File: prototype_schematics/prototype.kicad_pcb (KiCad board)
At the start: 2 copper layers, 3.7 x 6.9 mm, 98 parts, among them J1 AudioJack3, J2 Conn_01x04, J3 Conn_Coaxial, U1 MAX2608EUT+T, U10 TA0411A, U2 SPX3819M5-L, U3 TLV61046ADB, U4 MAX2680AUT+, U5 CD74HC4046A, U6 BGA2802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

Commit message: layout wip
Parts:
- J3: footprint Connector_Coaxial:SMA_Wurth_60312002114503_Vertical -> Connector_Coaxial:SMA_Samtec_SMA-J-P-X-ST-EM1_EdgeMount
- L12: footprint Inductor_SMD:L_0201_0603Metric_Pad0.64x0.40mm_HandSolder -> Inductor_SMD:L_0603_1608Metric_Pad1.05x0.95mm_HandSolder
- TP1, TP2, TP3, TP4, TP5, TP6: footprint CONMHF1_SMD_T:CONN_CONMHF1-SMD_LNX -> Connector_Coaxial:U.FL_Molex_MCRF_73412-0110_Vertical
- U6: footprint Package_TO_SOT_SMD:SOT-363_SC-70-6 -> Package_TO_SOT_SMD:SOT-363_SC-70-6_Handsoldering
- moved L12 86.9 mm to (61.5, 141.4), turned to 90 degrees
- moved U10 82.6 mm to (67.5, 139.0), turned to -90 degrees
- moved U9 82.0 mm to (60.9, 136.6), turned to 90 degrees
- moved TP5 78.6 mm to (71.5, 146.0), turned to 180 degrees
- moved C36 77.1 mm to (59.0, 134.5)
- moved C37 74.9 mm to (62.6, 138.8)
- moved L9 74.1 mm to (74.0, 139.0), turned to 180 degrees
- moved L8 73.3 mm to (77.5, 139.0), turned to 180 degrees
- moved RV2 72.4 mm to (62.0, 121.5), turned to 90 degrees
- moved C23 70.9 mm to (86.5, 141.6), turned to -90 degrees
- moved C38 67.9 mm to (71.5, 141.5), turned to -90 degrees
- moved L3 64.6 mm to (75.6, 120.5), turned to 180 degrees
- moved C16 64.0 mm to (80.0, 136.5), turned to 90 degrees
- moved C19 62.0 mm to (80.0, 141.5), turned to -90 degrees
- moved R15 60.7 mm to (83.5, 139.0), turned to 180 degrees
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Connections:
- C1 pad 2: Net-(U4-LO) -> Net-(TP1-In)
- C9 pad 2: Net-(TP1-In) -> Net-(U4-LO)
- R9 pad 1: Net-(Y1-OUT/IN) -> GND
- R9 pad 2: GND -> Net-(U5-SigIn)

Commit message: wip layout
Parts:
- added C40: 1nF, Capacitor_SMD:C_0603_1608Metric_Pad1.08x0.95mm_HandSolder, F.Cu at (101.5, 123.0)
- J2: footprint Connector_JST:JST_PH_S4B-PH-K_1x04_P2.00mm_Horizontal -> Connector_PinHeader_2.54mm:PinHeader_1x04_P2.54mm_Vertical
- moved TP6 90.8 mm to (63.0, 146.0), turned to 180 degrees
- moved C39 89.0 mm to (63.0, 141.5), turned to 90 degrees
- moved J1 77.9 mm to (63.2, 97.3), turned to 90 degrees
- moved U7 66.4 mm to (80.5, 97.5), turned to 180 degrees
- moved C29 59.1 mm to (80.5, 102.0)
- moved C27 58.7 mm to (97.5, 139.0), turned to -90 degrees
- moved TP3 58.0 mm to (86.5, 146.0), turned to 180 degrees
- moved TP4 52.4 mm to (97.5, 143.5), turned to 180 degrees
- moved L11 52.3 mm to (103.0, 134.5)
- moved JP3 51.1 mm to (88.5, 113.5), turned to 180 degrees
- moved JP2 51.0 mm to (88.5, 111.0), turned to 180 degrees
- moved JP1 51.0 mm to (88.5, 108.5), turned to 180 degrees
- moved C14 49.1 mm to (89.5, 120.0), turned to -90 degrees
- moved C21 45.3 mm to (100.0, 106.0)
- moved R8 43.4 mm to (89.5, 125.0), turned to -90 degrees
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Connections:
- C10 pad 2: Net-(Y1-OUT/IN) -> Net-(C10-Pad2)
- J2 pad 3: /AFOUT_P -> /AFOUT_N
- J2 pad 4: /AFOUT_N -> /AFOUT_P
- L5 pad 1: Net-(Y1-OUT/IN) -> Net-(C10-Pad2)
- R9 pad 1: GND -> Net-(Y1-OUT/IN)
- R9 pad 2: Net-(U5-SigIn) -> GND
- RV3 pad 1: Net-(R17-Pad2) -> Net-(R18-Pad1)
- RV3 pad 3: Net-(R18-Pad1) -> Net-(R17-Pad2)
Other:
- board size 3.7 x 6.9 mm -> 6.9 x 3.7 mm

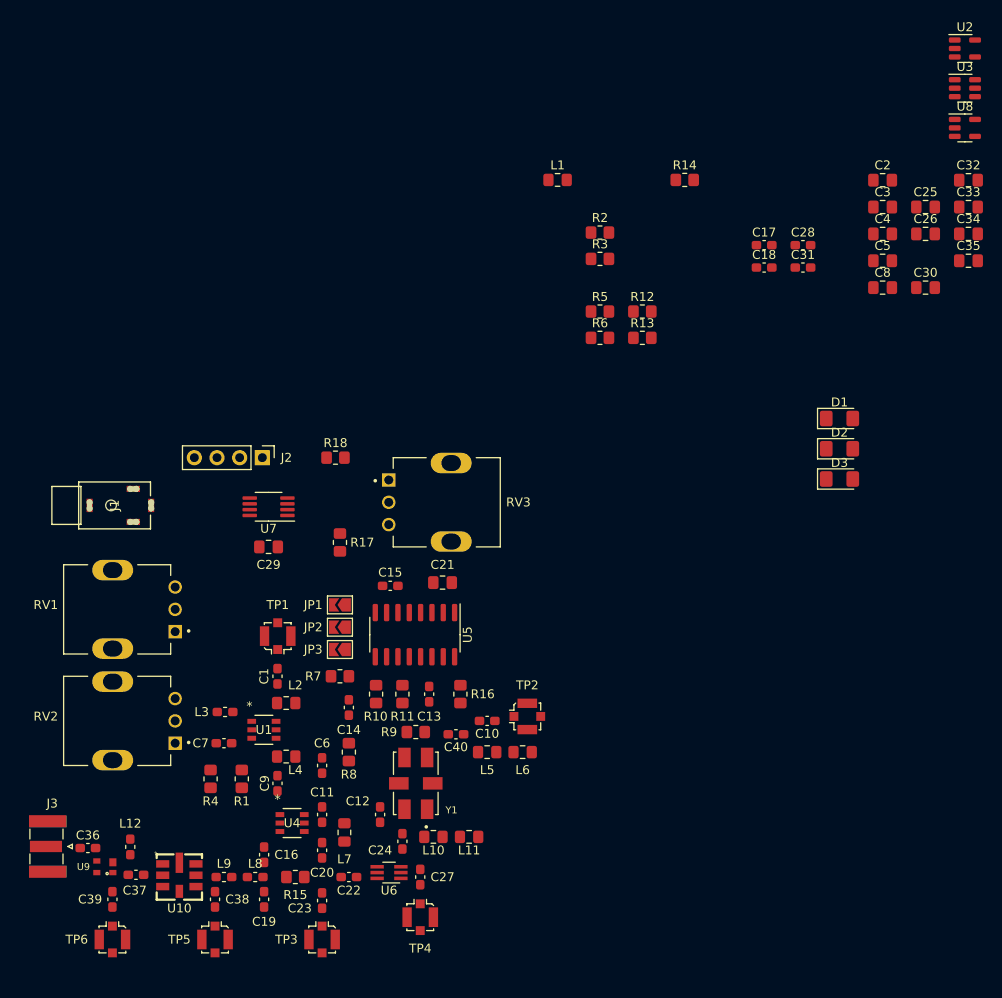
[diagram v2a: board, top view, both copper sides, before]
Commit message: preliminary layout finished
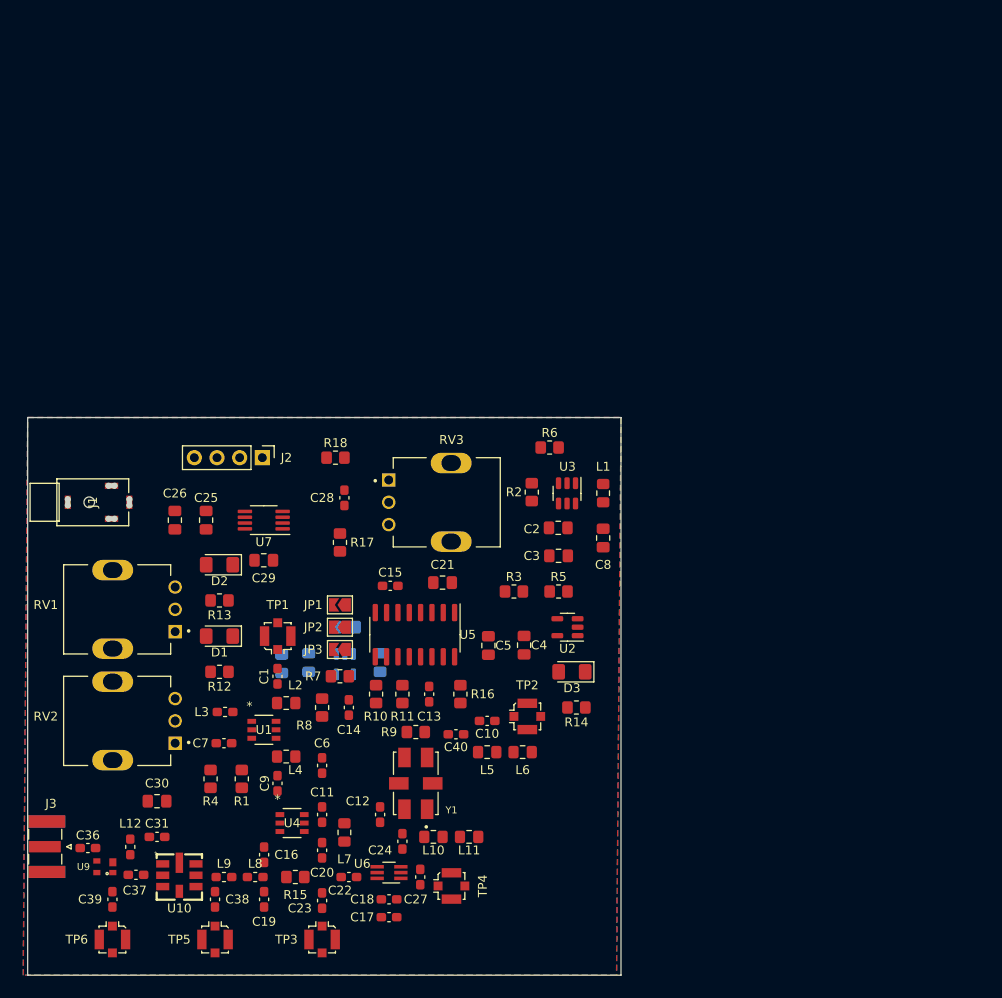
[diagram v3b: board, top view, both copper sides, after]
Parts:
- C32, C33, C34, C35, U8: moved to B.Cu
- moved C30 103.6 mm to (68.0, 130.5), turned to 180 degrees
- moved C31 96.5 mm to (68.0, 134.5), turned to 180 degrees
- moved U8 91.9 mm to (89.0, 115.1), turned to -90 degrees
- moved C26 90.0 mm to (70.0, 99.0), turned to -90 degrees
- moved C35 89.2 mm to (82.0, 115.1), turned to 90 degrees
- moved C34 88.2 mm to (85.0, 115.0), turned to 90 degrees
- moved C25 87.9 mm to (73.5, 99.0), turned to -90 degrees
- moved C17 86.3 mm to (94.0, 143.5), turned to 180 degrees
- moved C32 85.9 mm to (89.2, 111.0), turned to 180 degrees
- moved C33 83.4 mm to (93.0, 115.0), turned to 90 degrees
- moved C18 82.4 mm to (94.0, 141.5), turned to 180 degrees
- moved U2 78.7 mm to (114.0, 111.0), turned to 180 degrees
- moved D1 73.6 mm to (75.0, 112.0), turned to 180 degrees
- moved D2 70.7 mm to (75.0, 104.0), turned to 180 degrees
- moved U3 63.6 mm to (114.0, 96.0), turned to -90 degrees
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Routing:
- added copper zone on B.Cu, net GND
- added copper zone on F.Cu, net GND
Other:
- board size 6.9 x 3.7 mm -> 66.5 x 62.5 mm

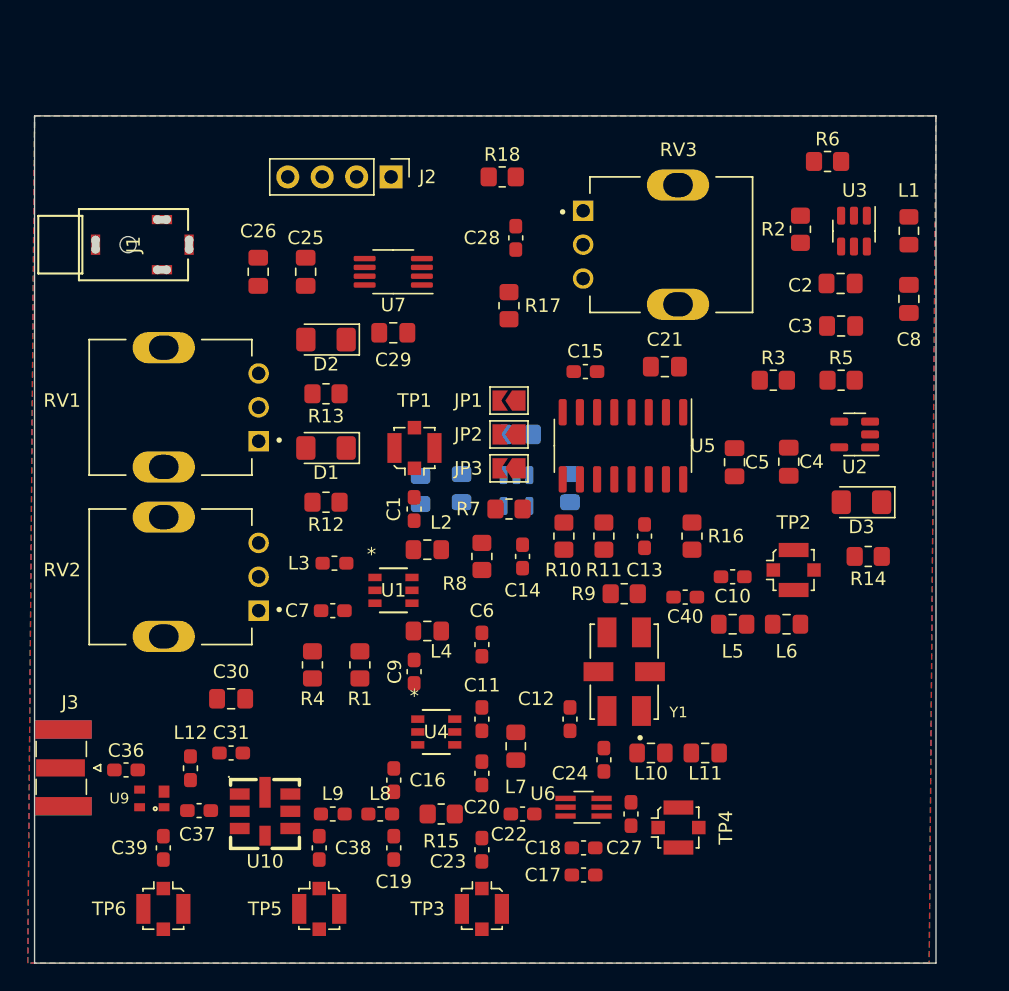
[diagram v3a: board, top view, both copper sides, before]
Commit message: layout adjustment and edge cut
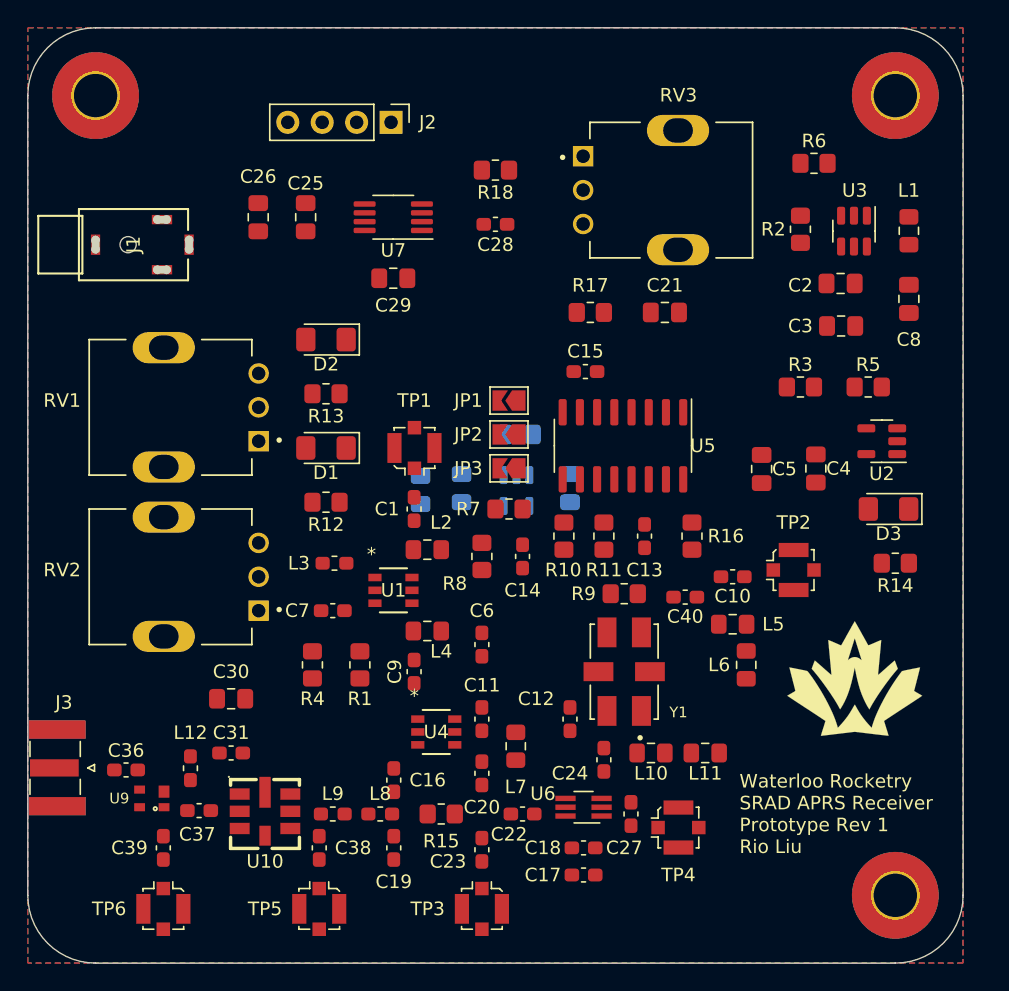
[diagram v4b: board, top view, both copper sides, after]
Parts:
- added G***: LOGO, Team_Logo:Logo_SilkScreen_10mm, F.Cu at (114.0, 129.0)
- added H1: MountingHole_Pad, MountingHole:MountingHole_3.2mm_M3_Pad_TopBottom, F.Cu at (58.0, 86.0)
- added H2: MountingHole_Pad, MountingHole:MountingHole_3.2mm_M3_Pad_TopBottom, F.Cu at (117.0, 86.0)
- added H3: MountingHole_Pad, MountingHole:MountingHole_3.2mm_M3_Pad_TopBottom, F.Cu at (117.0, 145.0)
- moved R17 6.02 mm to (94.5, 102.0), turned to 180 degrees
- moved L6 4.22 mm to (106.0, 128.0), turned to -90 degrees
- moved C25 4.03 mm to (73.5, 95.0)
- moved C26 4.03 mm to (70.0, 95.0)
- moved C29 4.03 mm to (80.0, 99.5)
- moved J2 4.03 mm to (79.8, 88.0)
- moved RV3 4.03 mm to (101.0, 93.0)
- moved U7 4.03 mm to (80.0, 95.0)
- moved C21 4.00 mm to (100.0, 102.0)
- moved C4 2.06 mm to (111.1, 113.5)
- moved C5 2.06 mm to (107.1, 113.5)
- moved D3 2.06 mm to (116.5, 116.5)
- moved R14 2.06 mm to (117.0, 120.5)
- moved R3 2.06 mm to (110.0, 107.5)
- moved R5 2.06 mm to (115.0, 107.5)
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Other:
- board size 66.5 x 62.5 mm -> 69 x 69 mm
- board text added: "Waterloo Rocketry SRAD APRS Receiver Prototype Rev 1 Rio Liu"

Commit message: wip routing
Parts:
- moved R16 23.9 mm to (83.0, 104.0), turned to 180 degrees
- moved C21 12.5 mm to (87.5, 101.5), turned to 180 degrees
- moved U7 6.48 mm to (73.8, 93.0)
- moved C29 6.47 mm to (80.5, 93.0), turned to 180 degrees
- moved C25 4.20 mm to (75.8, 98.5)
- moved C26 4.20 mm to (72.2, 98.5)
- moved JP2 2.50 mm to (88.5, 113.5)
- moved JP3 2.50 mm to (88.5, 111.0)
- moved R17 2.06 mm to (92.5, 101.5), turned to 0 degrees
- moved C12 2.00 mm to (91.0, 132.0)
- moved R15 2.00 mm to (83.5, 137.0)
- moved C6 1.92 mm to (85.6, 124.8)
- moved J2 1.47 mm to (79.8, 86.5)
- moved C2 1.36 mm to (111.6, 99.9)
- moved C3 1.36 mm to (111.6, 103.0)
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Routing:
- net +5V: track 0.00 -> 103.7 mm, vias 0 -> 2
- net +3V3: track 0.00 -> 41.4 mm, vias 0 -> 4
- net +6V: track 0.00 -> 32.9 mm
- net Net-(U5-SFout): track 0.00 -> 29.3 mm
- net Net-(R1-Pad1): track 0.00 -> 28.2 mm
- net Net-(U2-EN): track 0.00 -> 26.9 mm
- net /AFOUT_N: track 0.00 -> 23.7 mm
- net Net-(U7--): track 0.00 -> 21.0 mm
- net Net-(JP3-A): track 0.00 -> 12.8 mm
- net Net-(JP1-A): track 0.00 -> 12.6 mm
- net Net-(JP2-A): track 0.00 -> 10.7 mm
- net Net-(U1-TUNE): track 0.00 -> 10.2 mm
- net Net-(Y1-OUT/IN): track 0.00 -> 9.30 mm
- net Net-(R4-Pad1): track 0.00 -> 9.14 mm
- net Net-(JP1-B): track 0.00 -> 8.11 mm
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
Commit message: finish routing
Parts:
- added H4: MountingHole_Pad, MountingHole:MountingHole_3.2mm_M3_Pad_TopBottom, F.Cu at (58.0, 145.0)
- J1: footprint SJ1_2503A:CONN_SJ1-2503A -> SJ1_2503A:CUI_SJ1-2503A
- moved C34 21.5 mm to (74.8, 96.0), turned to 180 degrees
- moved C32 21.5 mm to (79.7, 91.8), turned to 0 degrees
- moved C33 21.2 mm to (83.5, 96.0)
- moved U8 21.2 mm to (79.5, 96.2)
- moved C35 17.6 mm to (74.8, 99.0), turned to 180 degrees
- moved J2 17.2 mm to (68.0, 99.0), turned to 180 degrees
- moved C6 9.52 mm to (77.9, 119.2), turned to 180 degrees
- moved J1 3.53 mm to (57.6, 95.5)
- moved TP6 2.50 mm to (65.5, 146.0)
- moved G*** 1.77 mm to (113.8, 130.8)
- moved TP2 0.70 mm to (110.2, 121.0)
- moved C27 0.66 mm to (97.5, 138.6)
- moved TP4 0.66 mm to (101.0, 139.6)
- moved C22 0.12 mm to (88.9, 138.5)
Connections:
- J2 pad 3: /AFOUT_N -> /AFOUT_P
- J2 pad 4: /AFOUT_P -> /AFOUT_N
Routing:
- net +3V3: track 41.4 -> 219.0 mm, vias 4 -> 1
- net GND: track 5.58 -> 20.5 mm, vias 1 -> 60
- net /AFOUT_P: track 0.00 -> 14.5 mm
- net /AFOUT_N: track 23.7 -> 36.4 mm
- net +5V: track 103.7 -> 114.4 mm, vias 2 -> 1
- net Net-(U10-IN): track 0.00 -> 2.16 mm
- net Net-(U5-FOUT): track 0.00 -> 1.27 mm
- net Net-(TP6-In): track 2.14 -> 3.39 mm
- net Net-(TP2-In): track 2.34 -> 3.04 mm
- net Net-(C24-Pad1): track 4.23 -> 4.89 mm

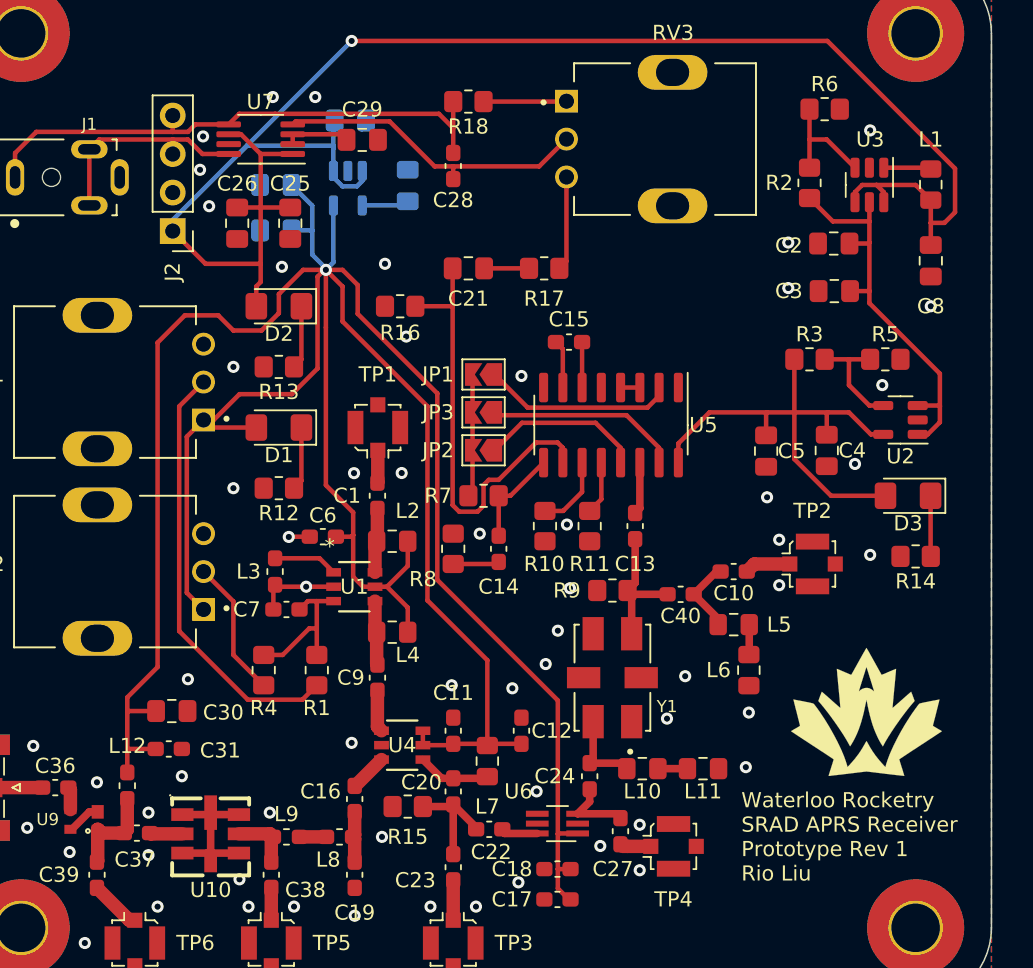
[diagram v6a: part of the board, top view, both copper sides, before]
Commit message: add a few more gnd vias
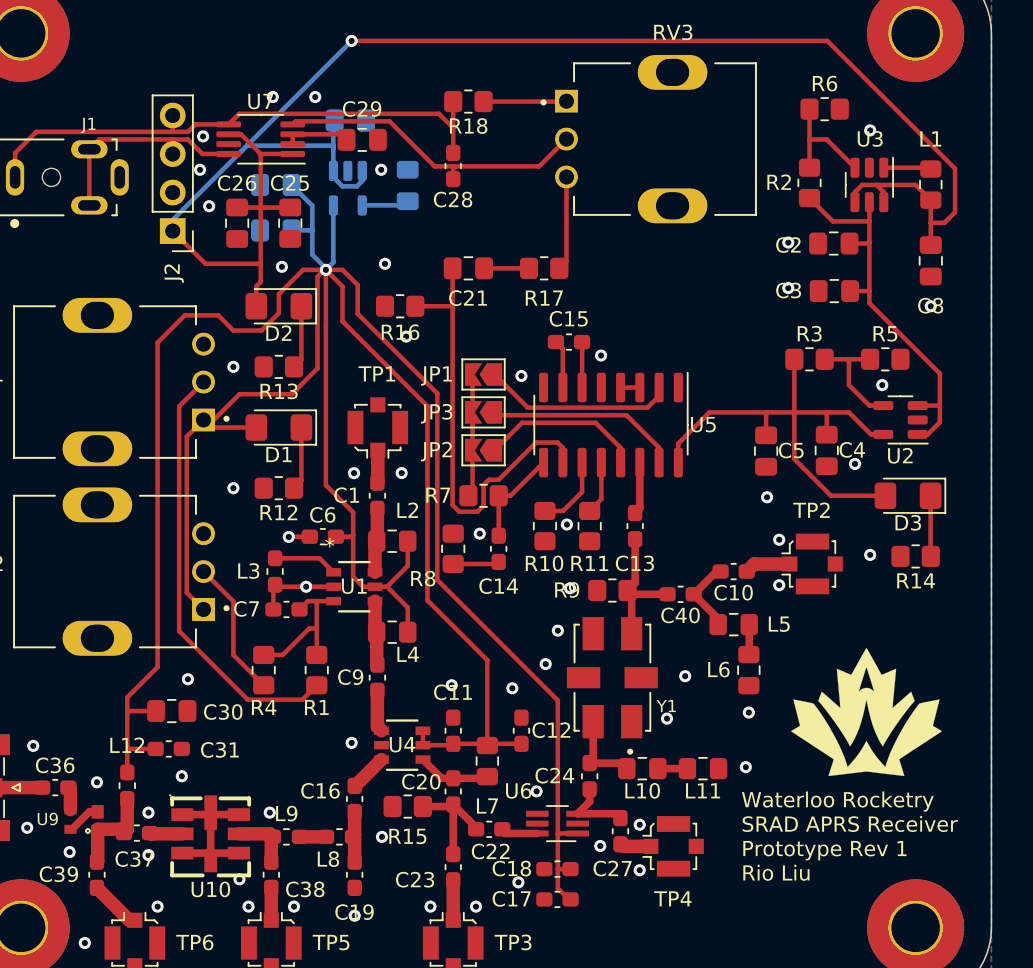
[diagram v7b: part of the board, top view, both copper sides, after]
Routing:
- net GND: vias 60 -> 62
